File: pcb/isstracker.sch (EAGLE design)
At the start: 24 parts, among them IC2 L7805CV, J1 MOTOR_RIGHT, J2 MOTOR, J3 MOTOR_LEFT, J4 DISPLAY, J6 CONTROL, J8 UART, J9 DISTANCE, Q2 60V/32A/35mΩ, U1 ARGON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

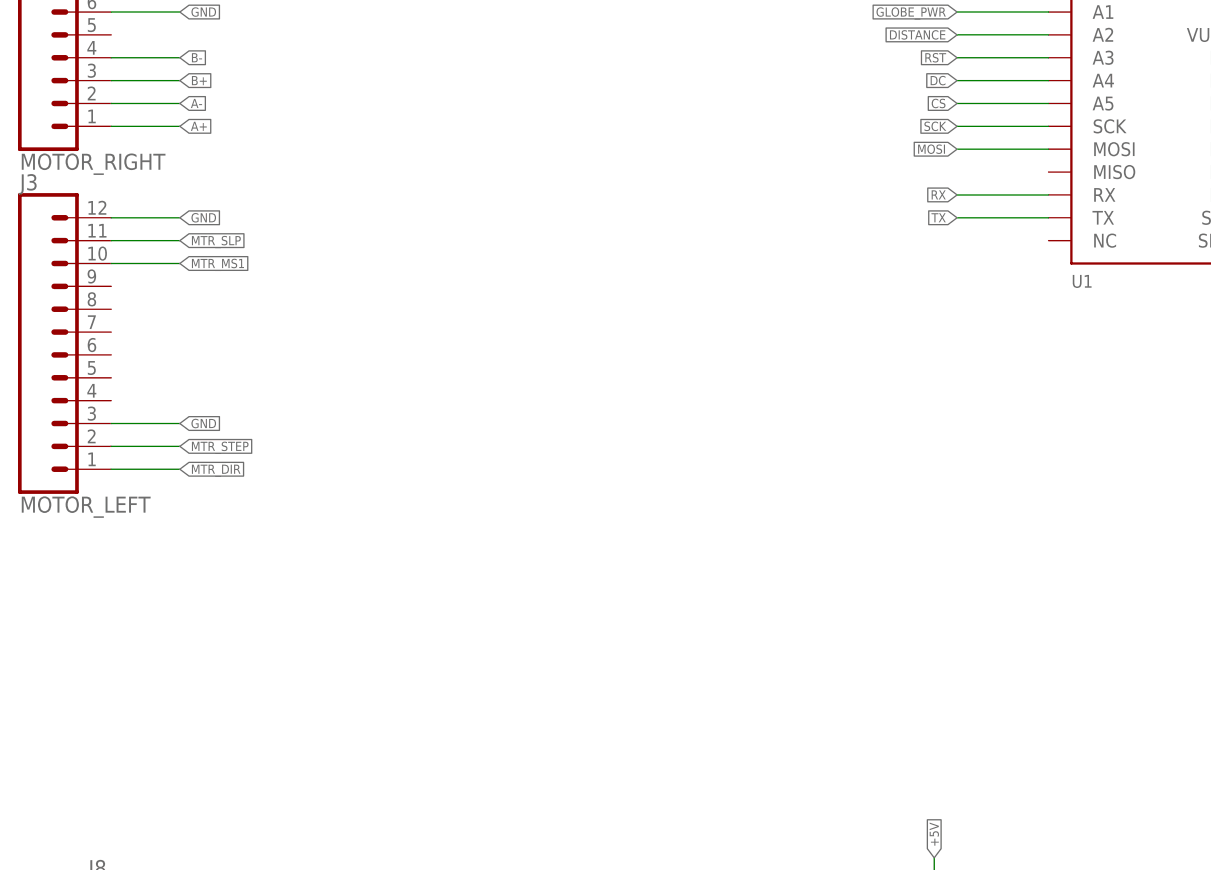
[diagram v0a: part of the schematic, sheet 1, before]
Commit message: Control board version 1.7
* Added a pushbutton to turn the globe back on
* Began to put globe power control back into app
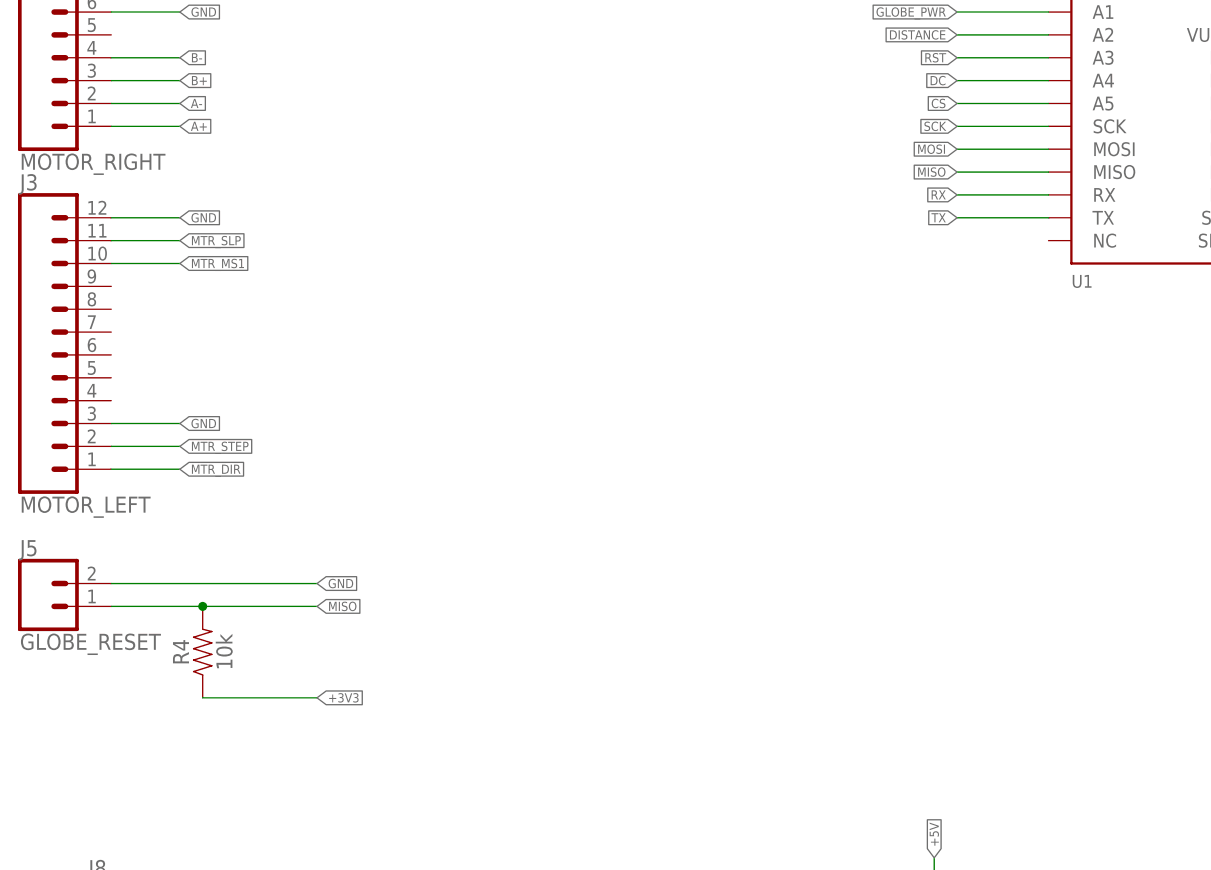
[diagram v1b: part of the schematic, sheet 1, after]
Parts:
- added J5: GLOBE_RESET, SparkFun-Connectors:CONN_02
- added R4: 10k, SparkFun-Resistors:0.75OHM-0805-1/4W-1%
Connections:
- new net MISO: J5.1, R4.2, U1.MISO
- net +3V3: now also R4.1
- net GND: now also J5.2
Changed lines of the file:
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@@
 <part name="LED3" library="adafruit" library_urn="urn:adsk.eagle:library:420" deviceset="LED" device="CHIPLED_1206" package3d_urn="urn:adsk.eagle:package:6240560/1" value="L171L-LPGC"/>
 <part name="LED1" library="adafruit" library_urn="urn:adsk.eagle:library:420" deviceset="LED" device="CHIPLED_1206" package3d_urn="urn:adsk.eagle:package:6240560/1" value="L171L-LPGC"/>
+<part name="J5" library="SparkFun-Connectors" library_urn="urn:adsk.eagle:library:513" deviceset="CONN_02" device="" package3d_urn="urn:adsk.eagle:package:38039/1" value="GLOBE_RESET"/>
+<part name="R4" library="SparkFun-Resistors" library_urn="urn:adsk.eagle:library:532" deviceset="0.75OHM" device="-0805-1/4W-1%" package3d_urn="urn:adsk.eagle:package:39651/1" value="10k"/>
 </parts>
 <sheets>
@@
 <attribute name="VALUE" x="159.512" y="71.755" size="1.778" layer="96" rot="R180"/>
 </instance>
+<instance part="J5" gate="G$1" x="12.7" y="116.84" smashed="yes">
+<attribute name="VALUE" x="10.16" y="112.014" size="1.778" layer="96" font="vector"/>
+<attribute name="NAME" x="10.16" y="122.428" size="1.778" layer="95" font="vector"/>
+</instance>
+<instance part="R4" gate="G$1" x="30.48" y="111.76" smashed="yes" rot="R90">
+<attribute name="NAME" x="28.956" y="111.76" size="1.778" layer="95" font="vector" rot="R90" align="bottom-center"/>
+<attribute name="VALUE" x="32.004" y="111.76" size="1.778" layer="96" font="vector" rot="R90" align="top-center"/>
+</instance>
 </instances>
 <busses>
@@
 <label x="27.94" y="160.02" size="1.016" layer="95" xref="yes"/>
 </segment>
+<segment>
+<pinref part="J5" gate="G$1" pin="2"/>
+<wire x1="20.32" y1="119.38" x2="43.18" y2="119.38" width="0.1524" layer="91"/>
+<label x="43.18" y="119.38" size="1.016" layer="95" xref="yes"/>
+</segment>
 </net>
 <net name="+5V" class="0">
@@
 <label x="238.76" y="149.86" size="1.016" layer="95" rot="R180" xref="yes"/>
 <pinref part="J9" gate="J$1" pin="1"/>
+</segment>
+<segment>
+<pinref part="R4" gate="G$1" pin="1"/>
+<wire x1="30.48" y1="106.68" x2="43.18" y2="106.68" width="0.1524" layer="91"/>
+<label x="43.18" y="106.68" size="1.016" layer="95" xref="yes"/>
 </segment>
 </net>
@@
 </segment>
 </net>
+<net name="MISO" class="0">
+<segment>
+<pinref part="U1" gate="U1" pin="MISO"/>
+<wire x1="124.46" y1="165.1" x2="114.3" y2="165.1" width="0.1524" layer="91"/>
+<label x="114.3" y="165.1" size="1.016" layer="95" rot="R180" xref="yes"/>
+</segment>
+<segment>
+<pinref part="J5" gate="G$1" pin="1"/>
+<wire x1="20.32" y1="116.84" x2="30.48" y2="116.84" width="0.1524" layer="91"/>
+<label x="43.18" y="116.84" size="1.016" layer="95" xref="yes"/>
+<pinref part="R4" gate="G$1" pin="2"/>
+<wire x1="30.48" y1="116.84" x2="43.18" y2="116.84" width="0.1524" layer="91"/>
+<junction x="30.48" y="116.84"/>
+</segment>
+</net>

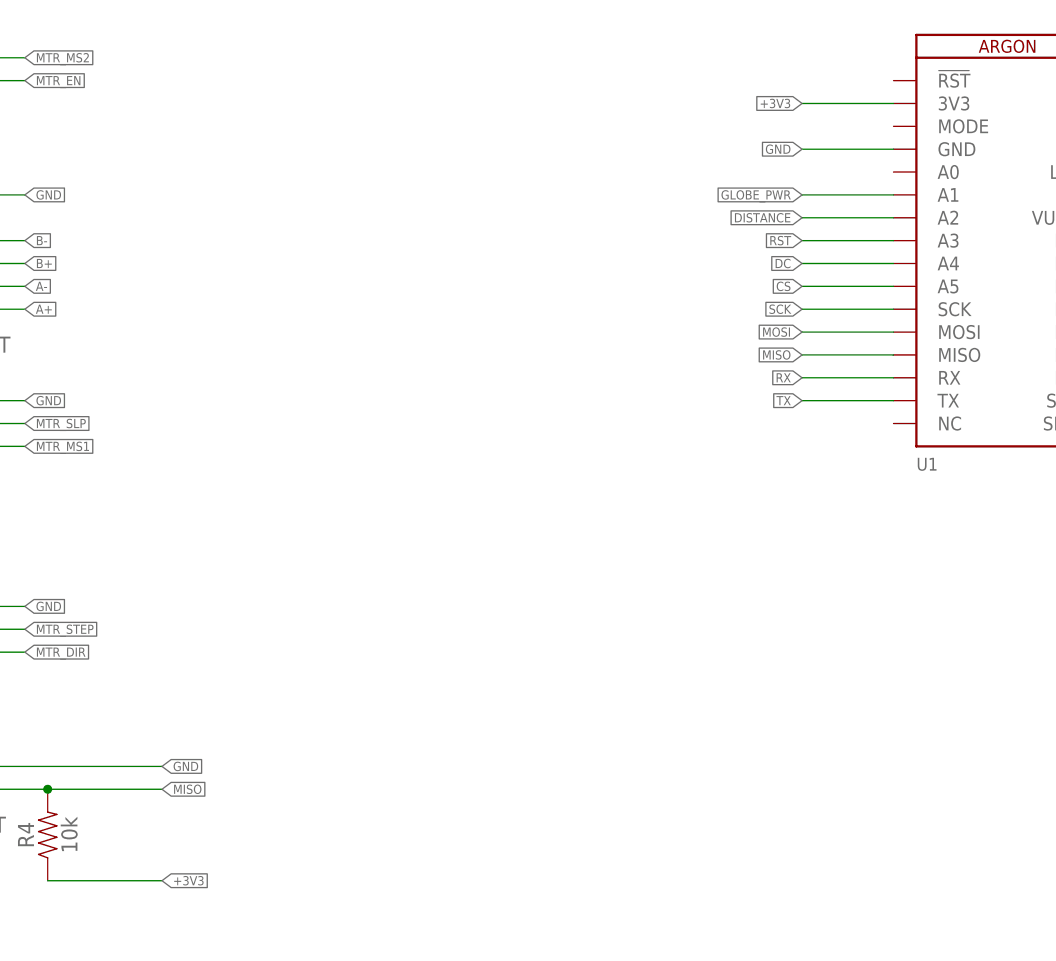
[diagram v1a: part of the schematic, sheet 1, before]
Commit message: Bump control board revision
* Move pins around for display, motion, and pushbutton
* Add pushbutton
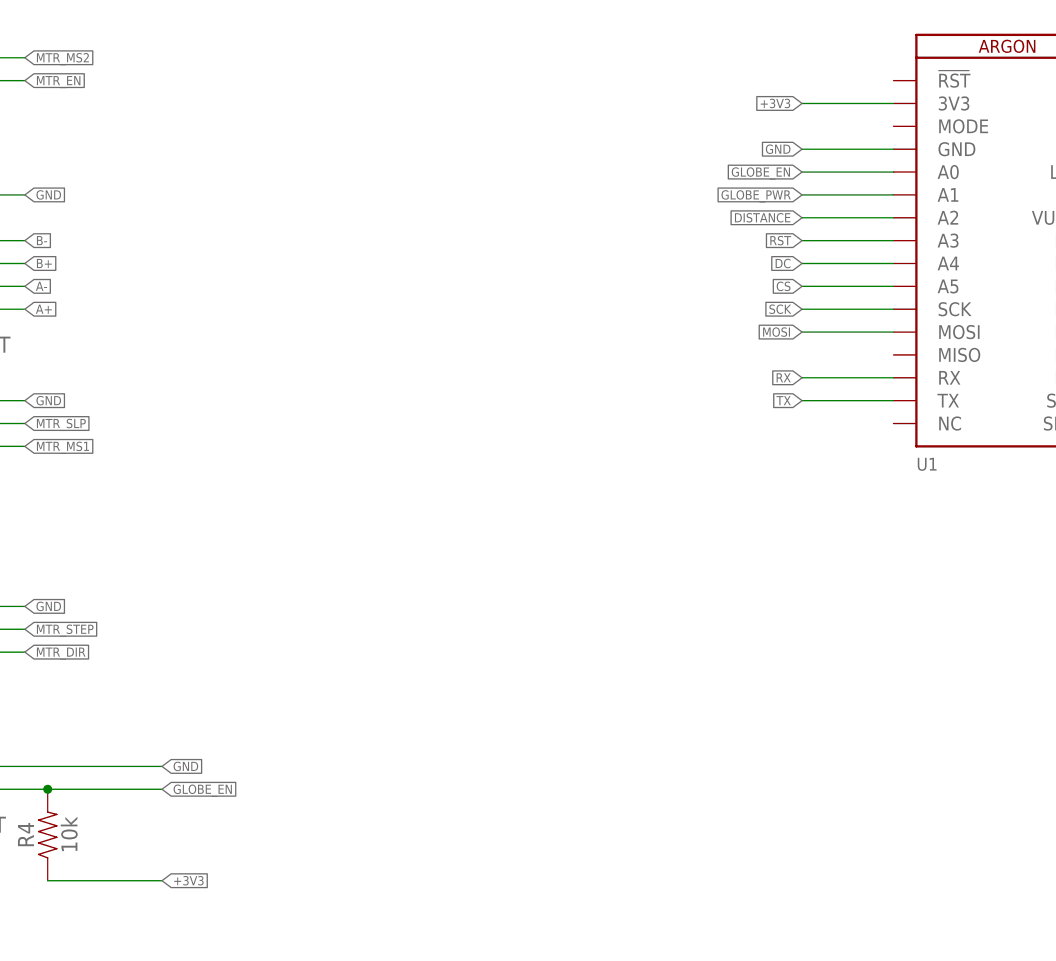
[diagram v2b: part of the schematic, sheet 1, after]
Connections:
- removed net MISO: J5.1, R4.2, U1.MISO
- new net GLOBE_EN: J5.1, R4.2, U1.A0
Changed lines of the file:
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@@
 </segment>
 </net>
-<net name="MISO" class="0">
+<net name="GLOBE_EN" class="0">
 <segment>
-<pinref part="U1" gate="U1" pin="MISO"/>
-<wire x1="124.46" y1="165.1" x2="114.3" y2="165.1" width="0.1524" layer="91"/>
-<label x="114.3" y="165.1" size="1.016" layer="95" rot="R180" xref="yes"/>
+<pinref part="U1" gate="U1" pin="A0"/>
+<wire x1="124.46" y1="185.42" x2="114.3" y2="185.42" width="0.1524" layer="91"/>
+<label x="114.3" y="185.42" size="1.016" layer="95" rot="R180" xref="yes"/>
 </segment>
 <segment>
